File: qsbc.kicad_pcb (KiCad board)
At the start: 6 copper layers, 80 x 80 mm, 126 parts, among them J1 USB_C_Receptacle_USB2.0, J2 USB_C_Receptacle_USB2.0, J3 USB_C_Receptacle_USB2.0, J4 ARJM11D7-502-AB-EW2, J7 USB_C_Receptacle_USB2.0, J8 Bus_M.2_Socket_M, U1 MIMX8MM6DVTLZAA, U10 TUSB320LI, U11 CH343P, U12 TPD4EUSB30, U13 TPD4EUSB30, U14 TPD4EUSB30, U15 W25Q32JVZP, U16 BD71847MWV, U18 RTL8211F, U19 NX5P3363, U2 74LVC1G04, U21 INA231, U3 MT40A1G16KD-062E, U4 TPD4EUSB30, U5 NX5P3363, U6 TUSB320LI, U8 74LVC1G04, U9 TPD4EUSB30, Y1 Crystal

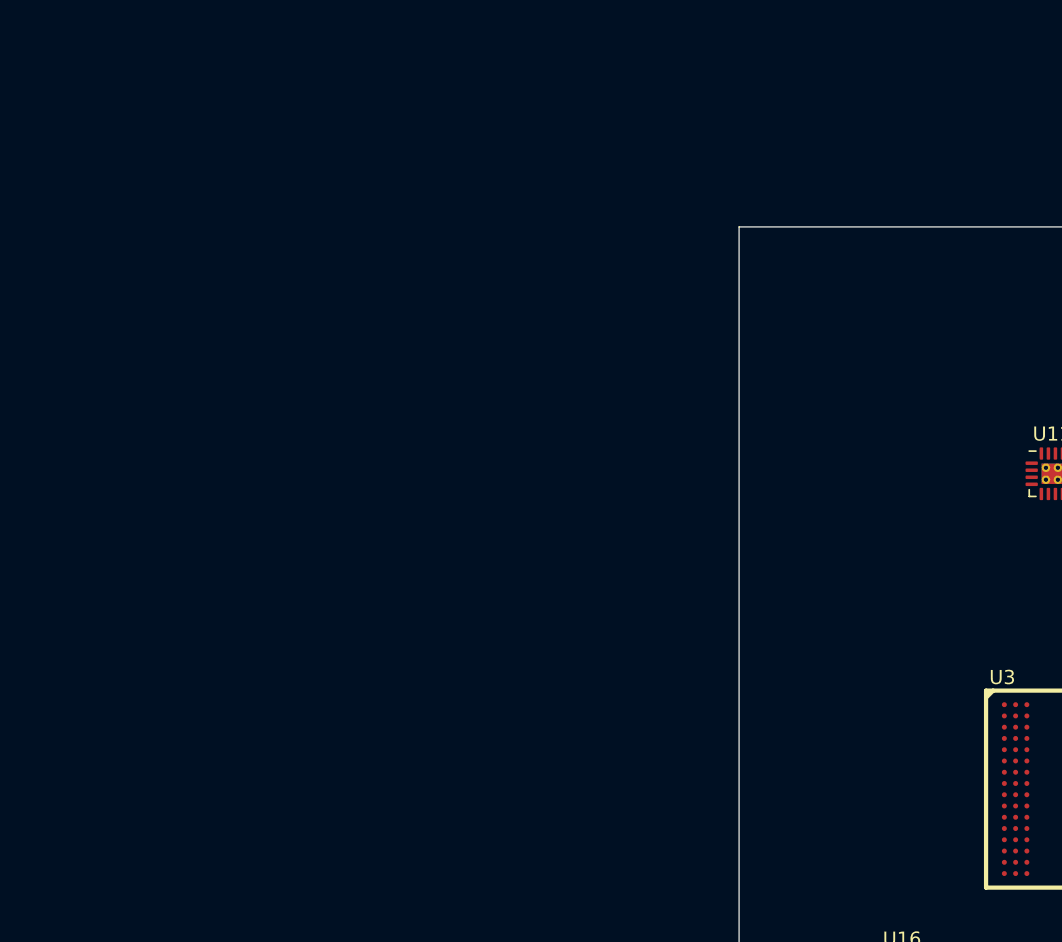
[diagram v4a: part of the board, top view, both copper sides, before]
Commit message: pcie done, misc fixes for usb, enet
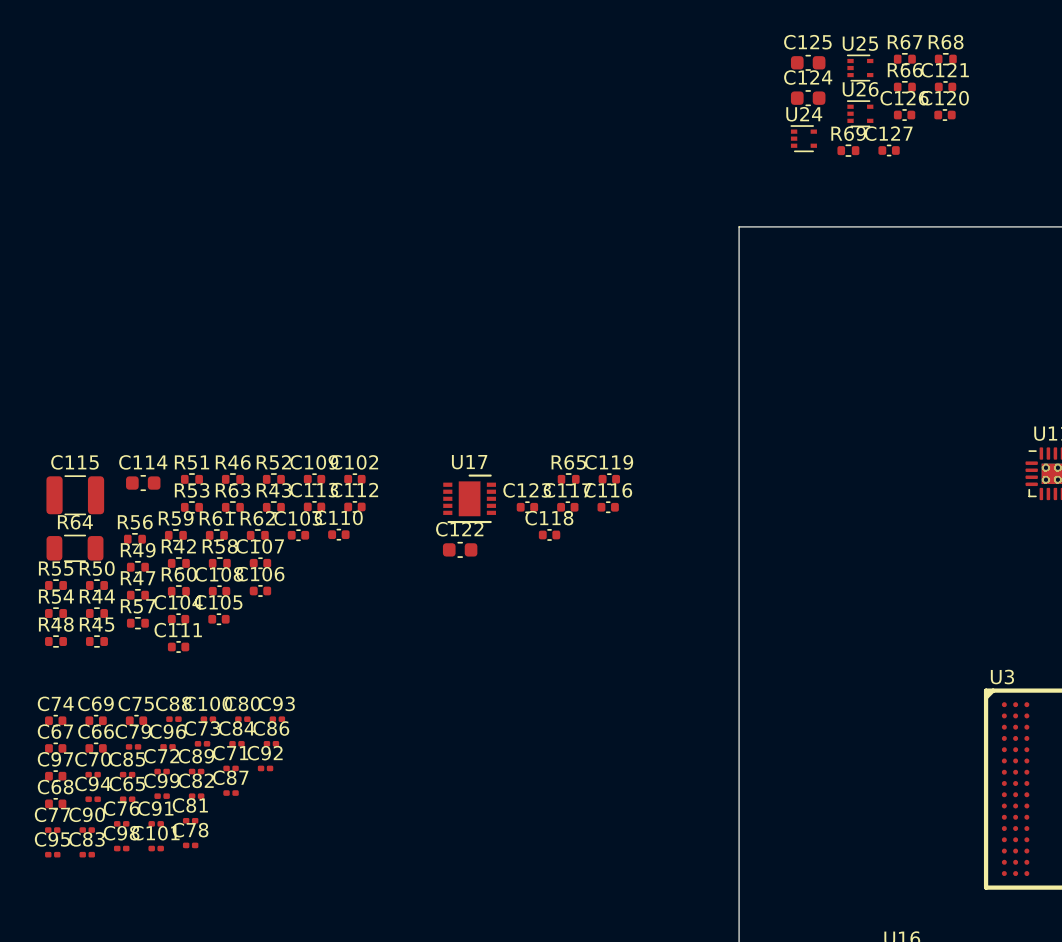
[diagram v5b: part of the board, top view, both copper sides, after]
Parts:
- added C100: 0.22uF, Capacitor_SMD:C_0201_0603Metric, F.Cu at (70.2, 93.9)
- added C101: 0.22uF, Capacitor_SMD:C_0201_0603Metric, F.Cu at (66.5, 103.1)
- added C102: 0.1uF, Capacitor_SMD:C_0402_1005Metric, F.Cu at (80.6, 76.9)
- added C103: 0.1uF, Capacitor_SMD:C_0402_1005Metric, F.Cu at (76.6, 80.8)
- added C104: 0.1uF, Capacitor_SMD:C_0402_1005Metric, F.Cu at (68.1, 86.8)
- added C105: 0.1uF, Capacitor_SMD:C_0402_1005Metric, F.Cu at (71.0, 86.8)
- added C106: 4.7uF, Capacitor_SMD:C_0402_1005Metric, F.Cu at (73.9, 84.8)
- added C107: 0.1uF, Capacitor_SMD:C_0402_1005Metric, F.Cu at (73.9, 82.8)
- added C108: 0.1uF, Capacitor_SMD:C_0402_1005Metric, F.Cu at (71.0, 84.8)
- added C109: 0.1uF, Capacitor_SMD:C_0402_1005Metric, F.Cu at (77.8, 76.9)
- added C110: C, Capacitor_SMD:C_0402_1005Metric, F.Cu at (79.5, 80.8)
- added C111: 0.1uF, Capacitor_SMD:C_0402_1005Metric, F.Cu at (68.1, 88.8)
- added C112: C, Capacitor_SMD:C_0402_1005Metric, F.Cu at (80.6, 78.8)
- added C113: 0.1uF, Capacitor_SMD:C_0402_1005Metric, F.Cu at (77.8, 78.8)
- added C114: 0.01uF, Capacitor_SMD:C_0603_1608Metric, F.Cu at (65.6, 77.1)
- added C115: 1000pF, Capacitor_SMD:C_1210_3225Metric, F.Cu at (60.8, 78.0)
- added C116: 4.7uF, Capacitor_SMD:C_0402_1005Metric, F.Cu at (98.6, 78.8)
- added C117: 0.1uF, Capacitor_SMD:C_0402_1005Metric, F.Cu at (95.8, 78.8)
- added C118: 20pF, Capacitor_SMD:C_0402_1005Metric, F.Cu at (94.5, 80.8)
- added C119: 20pF, Capacitor_SMD:C_0402_1005Metric, F.Cu at (98.7, 76.9)
- added C120: 0.22uF, Capacitor_SMD:C_0402_1005Metric, F.Cu at (122.6, 51.0)
- added C121: 0.22uF, Capacitor_SMD:C_0402_1005Metric, F.Cu at (122.6, 49.0)
- added C122: 10uF, Capacitor_SMD:C_0603_1608Metric, F.Cu at (88.1, 81.9)
- added C123: 0.1uF, Capacitor_SMD:C_0402_1005Metric, F.Cu at (92.9, 78.8)
- added C124: 10uF, Capacitor_SMD:C_0603_1608Metric, F.Cu at (112.8, 49.8)
- added C125: 10uF, Capacitor_SMD:C_0603_1608Metric, F.Cu at (112.8, 47.3)
- added C126: 0.1uF, Capacitor_SMD:C_0402_1005Metric, F.Cu at (119.7, 51.0)
- added C127: 0.1uF, Capacitor_SMD:C_0402_1005Metric, F.Cu at (118.6, 53.5)
- added C65: 1uF, Capacitor_SMD:C_0201_0603Metric, F.Cu at (64.5, 99.6)
- added C66: 10uF, Capacitor_SMD:C_0402_1005Metric, F.Cu at (62.2, 96.0)
- added C67: 10uF, Capacitor_SMD:C_0402_1005Metric, F.Cu at (59.4, 96.0)
- added C68: 10uF, Capacitor_SMD:C_0402_1005Metric, F.Cu at (59.4, 99.9)
- added C69: 10uF, Capacitor_SMD:C_0402_1005Metric, F.Cu at (62.2, 94.0)
- added C70: 1uF, Capacitor_SMD:C_0201_0603Metric, F.Cu at (62.0, 97.8)
- added C71: 0.22uF, Capacitor_SMD:C_0201_0603Metric, F.Cu at (71.8, 97.4)
- added C72: 1uF, Capacitor_SMD:C_0201_0603Metric, F.Cu at (66.9, 97.6)
- added C73: 1uF, Capacitor_SMD:C_0201_0603Metric, F.Cu at (69.8, 95.7)
- added C74: 10uF, Capacitor_SMD:C_0402_1005Metric, F.Cu at (59.4, 94.0)
- added C75: 10uF, Capacitor_SMD:C_0402_1005Metric, F.Cu at (65.1, 94.0)
- added C76: 1uF, Capacitor_SMD:C_0201_0603Metric, F.Cu at (64.1, 101.3)
- added C77: 1uF, Capacitor_SMD:C_0201_0603Metric, F.Cu at (59.2, 101.8)
- added C78: 1uF, Capacitor_SMD:C_0201_0603Metric, F.Cu at (69.0, 102.9)
- added C79: 1uF, Capacitor_SMD:C_0201_0603Metric, F.Cu at (64.9, 95.9)
- added C80: 0.22uF, Capacitor_SMD:C_0201_0603Metric, F.Cu at (72.7, 93.9)
- added C81: 1uF, Capacitor_SMD:C_0201_0603Metric, F.Cu at (69.0, 101.1)
- added C82: 1uF, Capacitor_SMD:C_0201_0603Metric, F.Cu at (69.4, 99.4)
- added C83: 1uF, Capacitor_SMD:C_0201_0603Metric, F.Cu at (61.6, 103.5)
- added C84: 1uF, Capacitor_SMD:C_0201_0603Metric, F.Cu at (72.3, 95.7)
- added C85: 1uF, Capacitor_SMD:C_0201_0603Metric, F.Cu at (64.5, 97.8)
- added C86: 1uF, Capacitor_SMD:C_0201_0603Metric, F.Cu at (74.7, 95.7)
- added C87: 1uF, Capacitor_SMD:C_0201_0603Metric, F.Cu at (71.8, 99.2)
- added C88: 1uF, Capacitor_SMD:C_0201_0603Metric, F.Cu at (67.8, 93.9)
- added C89: 1uF, Capacitor_SMD:C_0201_0603Metric, F.Cu at (69.4, 97.6)
- added C90: 1uF, Capacitor_SMD:C_0201_0603Metric, F.Cu at (61.6, 101.8)
- added C91: 1uF, Capacitor_SMD:C_0201_0603Metric, F.Cu at (66.5, 101.3)
- added C92: 1uF, Capacitor_SMD:C_0201_0603Metric, F.Cu at (74.3, 97.4)
- added C93: 1uF, Capacitor_SMD:C_0201_0603Metric, F.Cu at (75.1, 93.9)
- added C94: 1uF, Capacitor_SMD:C_0201_0603Metric, F.Cu at (62.0, 99.6)
- added C95: 1uF, Capacitor_SMD:C_0201_0603Metric, F.Cu at (59.2, 103.5)
- added C96: 1uF, Capacitor_SMD:C_0201_0603Metric, F.Cu at (67.4, 95.9)
- added C97: 10uF, Capacitor_SMD:C_0402_1005Metric, F.Cu at (59.4, 98.0)
- added C98: 0.22uF, Capacitor_SMD:C_0201_0603Metric, F.Cu at (64.1, 103.1)
- added C99: 0.22uF, Capacitor_SMD:C_0201_0603Metric, F.Cu at (66.9, 99.4)
- added R42: 4.7K, Resistor_SMD:R_0402_1005Metric, F.Cu at (68.1, 82.8)
- added R43: 4.7K, Resistor_SMD:R_0402_1005Metric, F.Cu at (74.9, 78.9)
- added R44: 4.7K, Resistor_SMD:R_0402_1005Metric, F.Cu at (62.3, 86.4)
- added R45: 4.7K, Resistor_SMD:R_0402_1005Metric, F.Cu at (62.3, 88.4)
- added R46: 4.7K, Resistor_SMD:R_0402_1005Metric, F.Cu at (72.0, 76.9)
- added R47: 4.7K, Resistor_SMD:R_0402_1005Metric, F.Cu at (65.2, 85.1)
- added R48: 4.7K, Resistor_SMD:R_0402_1005Metric, F.Cu at (59.4, 88.4)
- added R49: 4.7K, Resistor_SMD:R_0402_1005Metric, F.Cu at (65.2, 83.1)
- added R50: 4.7K, Resistor_SMD:R_0402_1005Metric, F.Cu at (62.3, 84.4)
- added R51: 1.5K, Resistor_SMD:R_0402_1005Metric, F.Cu at (69.1, 76.9)
- added R52: 0R, Resistor_SMD:R_0402_1005Metric, F.Cu at (74.9, 76.9)
- added R53: 0R, Resistor_SMD:R_0402_1005Metric, F.Cu at (69.1, 78.9)
- added R54: 0R, Resistor_SMD:R_0402_1005Metric, F.Cu at (59.4, 86.4)
- added R55: 0R, Resistor_SMD:R_0402_1005Metric, F.Cu at (59.4, 84.4)
- added R56: 0R, Resistor_SMD:R_0402_1005Metric, F.Cu at (65.0, 81.1)
- added R57: 2.49K, Resistor_SMD:R_0402_1005Metric, F.Cu at (65.2, 87.1)
- added R58: 4.7K, Resistor_SMD:R_0402_1005Metric, F.Cu at (71.0, 82.8)
- added R59: 4.7K, Resistor_SMD:R_0402_1005Metric, F.Cu at (67.9, 80.8)
- added R60: 4.7K, Resistor_SMD:R_0402_1005Metric, F.Cu at (68.1, 84.8)
- added R61: 4.7K, Resistor_SMD:R_0402_1005Metric, F.Cu at (70.8, 80.8)
- added R62: 470R, Resistor_SMD:R_0402_1005Metric, F.Cu at (73.7, 80.8)
- added R63: 470R, Resistor_SMD:R_0402_1005Metric, F.Cu at (72.0, 78.9)
- added R64: 1M, Resistor_SMD:R_1206_3216Metric, F.Cu at (60.8, 81.8)
- added R65: 8,2K, Resistor_SMD:R_0402_1005Metric, F.Cu at (95.8, 76.9)
- added R66: 10K, Resistor_SMD:R_0402_1005Metric, F.Cu at (119.7, 49.0)
- added R67: 10K, Resistor_SMD:R_0402_1005Metric, F.Cu at (119.7, 47.0)
- added R68: 10K, Resistor_SMD:R_0402_1005Metric, F.Cu at (122.6, 47.0)
- added R69: 10K, Resistor_SMD:R_0402_1005Metric, F.Cu at (115.7, 53.5)
- added U17: SI52112-B5-GM2, Package_DFN_QFN:DFN-10-1EP_3x3mm_P0.5mm_EP1.55x2.48mm, F.Cu at (88.8, 78.2)
- added U24: 74LVC1G07, Package_TO_SOT_SMD:SOT-553, F.Cu at (112.5, 52.7)
- added U25: 74LVC1G07, Package_TO_SOT_SMD:SOT-553, F.Cu at (116.6, 47.6)
- added U26: 74LVC1G07, Package_TO_SOT_SMD:SOT-553, F.Cu at (116.6, 50.9)
- U18: value RTL8211F -> RTL8211FD
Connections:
- net Net-(J8-Pad12) renamed VDD
- J4 pad 1: unconnected-(J4-Pad1) -> /Ethernet/TRD0_P
- J4 pad 10: unconnected-(J4-Pad10) -> /Ethernet/TRD3_N
- J4 pad 11: unconnected-(J4-Pad11) -> Net-(J4-Pad11)
- J4 pad 12: unconnected-(J4-Pad12) -> /Ethernet/ENET_LED2
- J4 pad 13: unconnected-(J4-Pad13) -> /Ethernet/ENET_LED1
- J4 pad 14: unconnected-(J4-Pad14) -> Net-(J4-Pad14)
- J4 pad 15: unconnected-(J4-Pad15) -> GNDPWR
- J4 pad 16: unconnected-(J4-Pad16) -> GNDPWR
- J4 pad 2: unconnected-(J4-Pad2) -> /Ethernet/TRD0_N
- J4 pad 3: unconnected-(J4-Pad3) -> /Ethernet/TRD1_P
- J4 pad 4: unconnected-(J4-Pad4) -> /Ethernet/TRD1_N
- J4 pad 5: unconnected-(J4-Pad5) -> Net-(J4-Pad5)
- J4 pad 6: unconnected-(J4-Pad6) -> Net-(J4-Pad5)
- J4 pad 7: unconnected-(J4-Pad7) -> /Ethernet/TRD2_P
- J4 pad 8: unconnected-(J4-Pad8) -> /Ethernet/TRD2_N
- J4 pad 9: unconnected-(J4-Pad9) -> /Ethernet/TRD3_P
- J8 pad 41: unconnected-(J8-Pad41) -> /PCIe/PCIE_RX_N
- J8 pad 43: unconnected-(J8-Pad43) -> /PCIe/PCIE_RX_P
- J8 pad 47: unconnected-(J8-Pad47) -> /PCIe/PCIE_TX_R_P
- J8 pad 49: unconnected-(J8-Pad49) -> /PCIe/PCIE_TX_R_N
- J8 pad 50: unconnected-(J8-Pad50) -> /PCIe/~{PCIE_RESET_3.3V}
- J8 pad 52: unconnected-(J8-Pad52) -> Net-(J8-Pad52)
- J8 pad 53: unconnected-(J8-Pad53) -> /PCIe/M2_REFCLK_N
- J8 pad 54: unconnected-(J8-Pad54) -> Net-(J8-Pad54)
- J8 pad 55: unconnected-(J8-Pad55) -> /PCIe/M2_REFCLK_P
- J8 pad 69: unconnected-(J8-Pad69) -> Net-(J8-Pad69)
- U1 pad A19: unconnected-(U1-PadA19) -> /PCIe/PCIE_RX_N
- U1 pad A20: unconnected-(U1-PadA20) -> /PCIe/PCIE_TX_N
- U1 pad A21: unconnected-(U1-PadA21) -> /PCIe/PCIE_REFCLK_P
- U1 pad AB27: unconnected-(U1-PadAB27) -> /Ethernet/ENET_MDIO
- U1 pad AC26: unconnected-(U1-PadAC26) -> /Ethernet/ENET_RD3
- U1 pad AC27: unconnected-(U1-PadAC27) -> /Ethernet/ENET_MDC
- U1 pad AD26: unconnected-(U1-PadAD26) -> /Ethernet/ENET_RD2
- U1 pad AD27: unconnected-(U1-PadAD27) -> /Ethernet/ENET_RD1
- U1 pad AE26: unconnected-(U1-PadAE26) -> /Ethernet/ENET_RXC
- U1 pad AE27: unconnected-(U1-PadAE27) -> /Ethernet/ENET_RD0
- U1 pad AF24: unconnected-(U1-PadAF24) -> /Ethernet/ENET_TX_CTL
- U1 pad AF25: unconnected-(U1-PadAF25) -> /Ethernet/ENET_TD3
- U1 pad AF26: unconnected-(U1-PadAF26) -> /Ethernet/ENET_TD1
- U1 pad AF27: unconnected-(U1-PadAF27) -> /Ethernet/ENET_RX_CTL
- U1 pad AG24: unconnected-(U1-PadAG24) -> /Ethernet/ENET_TXC
- U1 pad AG25: unconnected-(U1-PadAG25) -> /Ethernet/ENET_TD2
- U1 pad AG26: unconnected-(U1-PadAG26) -> /Ethernet/ENET_TD0
- U1 pad B19: unconnected-(U1-PadB19) -> /PCIe/PCIE_RX_P
- U1 pad B20: unconnected-(U1-PadB20) -> /PCIe/PCIE_TX_P
- U1 pad B21: unconnected-(U1-PadB21) -> /PCIe/PCIE_REFCLK_N
- U1 pad D19: unconnected-(U1-PadD19) -> /PCIe/PCIE_RESREF
- U1 pad J10: unconnected-(U1-PadJ10) -> /i.MX8MM Power/VDD_DRAM_xPU_0.9V
- U1 pad J11: unconnected-(U1-PadJ11) -> /i.MX8MM Power/NVCC_1.8V
- U1 pad J12: unconnected-(U1-PadJ12) -> /i.MX8MM Power/NVCC_1.8V
- U1 pad J22: unconnected-(U1-PadJ22) -> /i.MX8MM Power/NVCC_SNVS_1.8V
- U1 pad K12: unconnected-(U1-PadK12) -> /i.MX8MM Power/VDD_DRAM_xPU_0.9V
- U1 pad K13: unconnected-(U1-PadK13) -> /i.MX8MM Power/VDD_DRAM_xPU_0.9V
- U1 pad K15: /i.MX8MM Power/NVCC_DRAM -> /i.MX8MM Power/VDD_SOC_0.8V
- U1 pad K16: /i.MX8MM Power/NVCC_DRAM -> /i.MX8MM Power/VDD_SOC_0.8V
- U1 pad K22: unconnected-(U1-PadK22) -> /i.MX8MM Power/VDD_SNVS_0.8V
- U1 pad K8: unconnected-(U1-PadK8) -> /i.MX8MM Power/NVCC_DRAM_1.2V
- U1 pad K9: unconnected-(U1-PadK9) -> /i.MX8MM Power/NVCC_DRAM_1.2V
- U1 pad L10: unconnected-(U1-PadL10) -> /i.MX8MM Power/VDD_DRAM_xPU_0.9V
- U1 pad L11: unconnected-(U1-PadL11) -> /i.MX8MM Power/VDD_DRAM_xPU_0.9V
- U1 pad L13: unconnected-(U1-PadL13) -> /i.MX8MM Power/VDD_DRAM_xPU_0.9V
- U1 pad L15: /i.MX8MM Power/NVCC_DRAM -> /i.MX8MM Power/VDD_SOC_0.8V
- U1 pad L18: unconnected-(U1-PadL18) -> /i.MX8MM Power/VDD_SOC_0.8V
- U1 pad L19: unconnected-(U1-PadL19) -> /i.MX8MM Power/NVCC_1.8V
- U1 pad L9: unconnected-(U1-PadL9) -> /i.MX8MM Power/NVCC_DRAM_1.2V
- U1 pad M13: unconnected-(U1-PadM13) -> /i.MX8MM Power/VDD_DRAM_xPU_0.9V
- U1 pad M14: unconnected-(U1-PadM14) -> /i.MX8MM Power/VDD_DRAM_xPU_0.9V
- U1 pad M15: /i.MX8MM Power/NVCC_DRAM -> /i.MX8MM Power/VDD_SOC_0.8V
- U1 pad M19: unconnected-(U1-PadM19) -> /i.MX8MM Power/NVCC_1.8V
- U1 pad M9: unconnected-(U1-PadM9) -> /i.MX8MM Power/NVCC_DRAM_1.2V
- U1 pad N10: unconnected-(U1-PadN10) -> /i.MX8MM Power/VDD_DRAM_xPU_0.9V
- U1 pad N11: unconnected-(U1-PadN11) -> /i.MX8MM Power/VDD_DRAM_xPU_0.9V
- U1 pad N13: unconnected-(U1-PadN13) -> /i.MX8MM Power/VDD_SOC_0.8V
- U1 pad N15: /i.MX8MM Power/NVCC_DRAM -> /i.MX8MM Power/VDD_SOC_0.8V
- U1 pad N18: /i.MX8MM Power/VDD_SOC -> /i.MX8MM Power/VDD_SOC_0.8V
- U1 pad N19: unconnected-(U1-PadN19) -> /i.MX8MM Power/VDDA_1.8V
- U1 pad N8: unconnected-(U1-PadN8) -> /i.MX8MM Power/NVCC_DRAM_1.2V
- U1 pad N9: unconnected-(U1-PadN9) -> /i.MX8MM Power/NVCC_DRAM_1.2V
- U1 pad P12: unconnected-(U1-PadP12) -> /i.MX8MM Power/VDD_DRAM_xPU_0.9V
- U1 pad P5: unconnected-(U1-PadP5) -> /i.MX8MM Power/VDDA_1.8V
- U1 pad P7: unconnected-(U1-PadP7) -> /i.MX8MM Power/NVCC_DRAM_1.2V
- U1 pad P9: unconnected-(U1-PadP9) -> /i.MX8MM Power/VDD_DRAM_xPU_0.9V
- U1 pad R10: unconnected-(U1-PadR10) -> /i.MX8MM Power/VDD_DRAM_xPU_0.9V
- U1 pad R11: unconnected-(U1-PadR11) -> /i.MX8MM Power/VDD_DRAM_xPU_0.9V
- U1 pad R13: /i.MX8MM Power/VDD_SOC -> /i.MX8MM Power/VDD_ARM_0.9V
- U1 pad R15: /i.MX8MM Power/VDD_SOC -> /i.MX8MM Power/VDD_ARM_0.9V
- U1 pad R17: /i.MX8MM Power/NVCC_DRAM -> /i.MX8MM Power/VDD_SOC_0.8V
- U1 pad R18: /i.MX8MM Power/VDD_SOC -> /i.MX8MM Power/VDD_SOC_0.8V
- U1 pad R8: unconnected-(U1-PadR8) -> /i.MX8MM Power/NVCC_DRAM_1.2V
- U1 pad R9: unconnected-(U1-PadR9) -> /i.MX8MM Power/NVCC_DRAM_1.2V
- U1 pad T13: /i.MX8MM Power/VDD_SOC -> /i.MX8MM Power/VDD_ARM_0.9V
- U1 pad T14: /i.MX8MM Power/VDD_SOC -> /i.MX8MM Power/VDD_ARM_0.9V
- U1 pad T15: /i.MX8MM Power/VDD_SOC -> /i.MX8MM Power/VDD_ARM_0.9V
- U1 pad T9: unconnected-(U1-PadT9) -> /i.MX8MM Power/NVCC_DRAM_1.2V
- U1 pad U10: unconnected-(U1-PadU10) -> /i.MX8MM Power/VDD_DRAM_xPU_0.9V
- U1 pad U11: unconnected-(U1-PadU11) -> /i.MX8MM Power/VDD_DRAM_xPU_0.9V
- U1 pad U13: /i.MX8MM Power/VDD_SOC -> /i.MX8MM Power/VDD_ARM_0.9V
- U1 pad U15: /i.MX8MM Power/VDD_SOC -> /i.MX8MM Power/VDD_ARM_0.9V
- U1 pad U17: /i.MX8MM Power/NVCC_DRAM -> /i.MX8MM Power/VDD_SOC_0.8V
- U1 pad U18: /i.MX8MM Power/VDD_SOC -> /i.MX8MM Power/VDD_SOC_0.8V
- U1 pad U9: unconnected-(U1-PadU9) -> /i.MX8MM Power/NVCC_DRAM_1.2V
- U1 pad V12: unconnected-(U1-PadV12) -> /i.MX8MM Power/VDD_DRAM_xPU_0.9V
- U1 pad V13: /i.MX8MM Power/VDD_SOC -> /i.MX8MM Power/VDD_ARM_0.9V
- U1 pad V15: /i.MX8MM Power/VDD_SOC -> /i.MX8MM Power/VDD_ARM_0.9V
- U1 pad V16: /i.MX8MM Power/VDD_SOC -> /i.MX8MM Power/VDD_ARM_0.9V
- U1 pad V19: unconnected-(U1-PadV19) -> /i.MX8MM Power/NVCC_1.8V
- U1 pad V20: unconnected-(U1-PadV20) -> /i.MX8MM Power/NVCC_1.8V
- U1 pad V8: unconnected-(U1-PadV8) -> /i.MX8MM Power/NVCC_DRAM_1.2V
- U1 pad V9: unconnected-(U1-PadV9) -> /i.MX8MM Power/NVCC_DRAM_1.2V
- U1 pad W10: unconnected-(U1-PadW10) -> /i.MX8MM Power/VDD_DRAM_xPU_0.9V
- U1 pad W11: unconnected-(U1-PadW11) -> /i.MX8MM Power/VDD_DRAM_xPU_0.9V
- U1 pad W12: unconnected-(U1-PadW12) -> /i.MX8MM Power/NVCC_1.8V
- U1 pad W13: /i.MX8MM Power/VDD_SOC -> /i.MX8MM Power/VDD_ARM_0.9V
- U1 pad W14: /i.MX8MM Power/VDD_SOC -> /i.MX8MM Power/VDD_ARM_0.9V
- U1 pad W15: /i.MX8MM Power/VDD_SOC -> /i.MX8MM Power/VDD_ARM_0.9V
- U1 pad W16: /i.MX8MM Power/VDD_SOC -> /i.MX8MM Power/VDD_ARM_0.9V
- U13 pad 1: Net-(U13-Pad1) -> /Ethernet/TRD2_P
- U13 pad 10: Net-(U13-Pad1) -> /Ethernet/TRD2_P
- U13 pad 2: Net-(U13-Pad2) -> /Ethernet/TRD2_N
- U13 pad 3: Net-(U13-Pad3) -> GND
- U13 pad 4: Net-(U13-Pad4) -> /Ethernet/TRD3_P
- U13 pad 5: Net-(U13-Pad5) -> /Ethernet/TRD3_N
- U13 pad 6: Net-(U13-Pad5) -> /Ethernet/TRD3_N
- U13 pad 7: Net-(U13-Pad4) -> /Ethernet/TRD3_P
- U13 pad 8: Net-(U13-Pad3) -> GND
- U13 pad 9: Net-(U13-Pad2) -> /Ethernet/TRD2_N
- U14 pad 1: Net-(U14-Pad1) -> /Ethernet/TRD0_P
- U14 pad 10: Net-(U14-Pad1) -> /Ethernet/TRD0_P
- U14 pad 2: Net-(U14-Pad2) -> /Ethernet/TRD0_N
- U14 pad 3: Net-(U14-Pad3) -> GND
- U14 pad 4: Net-(U14-Pad4) -> /Ethernet/TRD1_P
- U14 pad 5: Net-(U14-Pad5) -> /Ethernet/TRD1_N
- U14 pad 6: Net-(U14-Pad5) -> /Ethernet/TRD1_N
- U14 pad 7: Net-(U14-Pad4) -> /Ethernet/TRD1_P
- U14 pad 8: Net-(U14-Pad3) -> GND
- U14 pad 9: Net-(U14-Pad2) -> /Ethernet/TRD0_N
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
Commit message: ddr: add dual die support, misc work
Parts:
- added C128: 0.1uF, Capacitor_SMD:C_0402_1005Metric, F.Cu at (314.2, 207.7)
- added C129: 0.1uF, Capacitor_SMD:C_0402_1005Metric, F.Cu at (320.1, 203.8)
- added C130: 0.1uF, Capacitor_SMD:C_0402_1005Metric, F.Cu at (318.4, 205.8)
- added C131: 18pF, Capacitor_SMD:C_0402_1005Metric, F.Cu at (320.2, 216.1)
- added C132: 10uF, Capacitor_SMD:C_0402_1005Metric, F.Cu at (315.0, 214.4)
- added C133: 0.1uF, Capacitor_SMD:C_0402_1005Metric, F.Cu at (313.1, 220.6)
- added C134: 0.1uF, Capacitor_SMD:C_0402_1005Metric, F.Cu at (316.0, 218.7)
- added C135: 1uF, Capacitor_SMD:C_0402_1005Metric, F.Cu at (317.3, 216.7)
- added C136: 0.1uF, Capacitor_SMD:C_0402_1005Metric, F.Cu at (316.0, 220.6)
- added C137: 0.1uF, Capacitor_SMD:C_0402_1005Metric, F.Cu at (329.8, 216.7)
- added C138: 0.1uF, Capacitor_SMD:C_0402_1005Metric, F.Cu at (329.8, 218.7)
- added C139: 0.22uF, Capacitor_SMD:C_0201_0603Metric, F.Cu at (317.1, 254.5)
- added C140: 10uF, Capacitor_SMD:C_0402_1005Metric, F.Cu at (314.4, 254.6)
- added C141: 0.22uF, Capacitor_SMD:C_0201_0603Metric, F.Cu at (319.1, 256.3)
- added C142: 0.22uF, Capacitor_SMD:C_0201_0603Metric, F.Cu at (319.5, 254.5)
- added C143: 0.22uF, Capacitor_SMD:C_0201_0603Metric, F.Cu at (316.7, 256.5)
- added C144: 0.22uF, Capacitor_SMD:C_0201_0603Metric, F.Cu at (314.2, 256.5)
- added C145: 2200pF, Capacitor_SMD:C_0402_1005Metric, F.Cu at (361.6, 181.5)
- added C146: 0.22uF, Capacitor_SMD:C_0201_0603Metric, F.Cu at (369.1, 181.2)
- added C147: 10uF, Capacitor_SMD:C_0402_1005Metric, F.Cu at (361.6, 179.5)
- added C148: 4.7uF, Capacitor_SMD:C_0402_1005Metric, F.Cu at (364.4, 179.5)
- added C149: 0.22uF, Capacitor_SMD:C_0201_0603Metric, F.Cu at (363.8, 185.1)
- added C150: 0.22uF, Capacitor_SMD:C_0201_0603Metric, F.Cu at (363.8, 183.3)
- added C151: 0.22uF, Capacitor_SMD:C_0201_0603Metric, F.Cu at (367.1, 179.4)
- added C152: 0.22uF, Capacitor_SMD:C_0201_0603Metric, F.Cu at (361.4, 185.1)
- added C153: 0.22uF, Capacitor_SMD:C_0201_0603Metric, F.Cu at (361.4, 183.3)
- added C154: 0.22uF, Capacitor_SMD:C_0201_0603Metric, F.Cu at (364.2, 181.4)
- added C155: 0.22uF, Capacitor_SMD:C_0201_0603Metric, F.Cu at (366.7, 181.4)
- added C156: 0.22uF, Capacitor_SMD:C_0201_0603Metric, F.Cu at (366.3, 183.1)
- added C157: 0.22uF, Capacitor_SMD:C_0201_0603Metric, F.Cu at (369.6, 179.4)
- added C158: 0.22uF, Capacitor_SMD:C_0201_0603Metric, F.Cu at (366.3, 184.9)
- added C159: 12pF, Capacitor_SMD:C_0402_1005Metric, F.Cu at (333.3, 272.9)
- added C160: 12pF, Capacitor_SMD:C_0402_1005Metric, F.Cu at (330.2, 276.9)
- added C19: 10uF, Capacitor_SMD:C_0603_1608Metric, F.Cu at (290.1, 234.1)
- added C20: 10uF, Capacitor_SMD:C_0603_1608Metric, F.Cu at (278.0, 231.6)
- added C21: 10uF, Capacitor_SMD:C_0603_1608Metric, F.Cu at (282.0, 239.1)
- added C22: 10uF, Capacitor_SMD:C_0603_1608Metric, F.Cu at (278.0, 234.1)
- added C23: 10uF, Capacitor_SMD:C_0603_1608Metric, F.Cu at (278.0, 236.6)
- added C24: 10uF, Capacitor_SMD:C_0603_1608Metric, F.Cu at (294.1, 231.6)
- added C25: 10uF, Capacitor_SMD:C_0603_1608Metric, F.Cu at (286.0, 241.6)
- added C26: 10uF, Capacitor_SMD:C_0603_1608Metric, F.Cu at (286.0, 239.1)
- added C33: 10uF, Capacitor_SMD:C_0603_1608Metric, F.Cu at (282.0, 231.6)
- added C34: 22uF, Capacitor_SMD:C_0603_1608Metric, F.Cu at (278.0, 239.1)
- added C35: 22uF, Capacitor_SMD:C_0603_1608Metric, F.Cu at (282.0, 236.6)
- added C36: 22uF, Capacitor_SMD:C_0603_1608Metric, F.Cu at (290.1, 231.6)
- added C37: 22uF, Capacitor_SMD:C_0603_1608Metric, F.Cu at (286.0, 231.6)
- added C38: 22uF, Capacitor_SMD:C_0603_1608Metric, F.Cu at (294.1, 234.1)
- added C39: 22uF, Capacitor_SMD:C_0603_1608Metric, F.Cu at (286.0, 236.6)
- added C40: 22uF, Capacitor_SMD:C_0603_1608Metric, F.Cu at (278.0, 241.6)
- added C41: 22uF, Capacitor_SMD:C_0603_1608Metric, F.Cu at (298.1, 231.6)
- added C42: 22uF, Capacitor_SMD:C_0603_1608Metric, F.Cu at (286.0, 234.1)
- added C43: 22uF, Capacitor_SMD:C_0603_1608Metric, F.Cu at (290.1, 236.6)
- added C44: 22uF, Capacitor_SMD:C_0603_1608Metric, F.Cu at (282.0, 234.1)
- added C46: 22uF, Capacitor_SMD:C_0603_1608Metric, F.Cu at (282.0, 241.6)
- added D2: LED_Orange, LED_SMD:LED_0603_1608Metric, F.Cu at (307.9, 207.4)
- added D3: LED_Yellow, LED_SMD:LED_0603_1608Metric, F.Cu at (327.4, 214.5)
- added H1: MountingHole_Pad, MountingHole:MountingHole_3.2mm_M3_Pad_Via, F.Cu at (111.9, 134.9)
- added H2: MountingHole_Pad, MountingHole:MountingHole_3.2mm_M3_Pad_Via, F.Cu at (183.9, 134.9)
- added H3: MountingHole_Pad, MountingHole:MountingHole_3.2mm_M3_Pad_Via, F.Cu at (111.9, 62.9)
- added H4: MountingHole_Pad, MountingHole:MountingHole_3.2mm_M3_Pad_Via, F.Cu at (183.9, 62.9)
- added H5: MountingHole_Pad, Mounting_Wuerth:Mounting_Wuerth_WA-SMSI-M3_H2.5mm_9774025360, F.Cu at (168.1, 101.3)
- added J5: Micro_SD_Card_Det1, qsbc:GCT_MEM2051-00-195-00-A_REVC, F.Cu at (139.4, 68.0)
- added J6: Conn_ARM_JTAG_SWD_10, Connector_PinHeader_1.27mm:PinHeader_2x05_P1.27mm_Vertical, F.Cu at (327.6, 202.5)
- added R1: 240R, Resistor_SMD:R_0201_0603Metric, F.Cu at (317.0, 232.9)
- added R10: 100K, Resistor_SMD:R_0402_1005Metric, F.Cu at (293.5, 236.3)
- added R100: 10K, Resistor_SMD:R_0402_1005Metric, F.Cu at (264.2, 156.4)
- added R101: 100K, Resistor_SMD:R_0402_1005Metric, F.Cu at (292.4, 238.8)
- added R102: 0R, Resistor_SMD:R_0402_1005Metric, F.Cu at (312.4, 270.9)
- added R103: 0R, Resistor_SMD:R_0402_1005Metric, F.Cu at (309.3, 277.0)
- added R104: 100K, Resistor_SMD:R_0402_1005Metric, F.Cu at (330.4, 270.9)
- added R105: 100K, Resistor_SMD:R_0402_1005Metric, F.Cu at (327.3, 277.0)
- added R106: 0R, Resistor_SMD:R_0402_1005Metric, F.Cu at (330.4, 274.9)
- added R107: 510K, Resistor_SMD:R_0402_1005Metric, F.Cu at (327.5, 272.9)
- added R108: 100K, Resistor_SMD:R_0402_1005Metric, F.Cu at (330.4, 272.9)
- added R109: 100K, Resistor_SMD:R_0402_1005Metric, F.Cu at (327.5, 274.9)
- added R11: 100K, Resistor_SMD:R_0402_1005Metric, F.Cu at (297.5, 233.8)
- added R110: 10K, Resistor_SMD:R_0402_1005Metric, F.Cu at (327.5, 270.9)
- added R111: 100K, Resistor_SMD:R_0402_1005Metric, F.Cu at (324.4, 277.0)
- added R112: 10K, Resistor_SMD:R_0402_1005Metric, F.Cu at (333.3, 270.9)
- added R113: 4.7K, Resistor_SMD:R_0402_1005Metric, F.Cu at (301.6, 286.4)
- added R114: 4.7K, Resistor_SMD:R_0402_1005Metric, F.Cu at (298.7, 286.4)
- added R15: 0R, Resistor_SMD:R_0402_1005Metric, F.Cu at (280.4, 252.5)
- added R16: 0R, Resistor_SMD:R_0402_1005Metric, F.Cu at (287.8, 248.1)
- added R2: 240R, Resistor_SMD:R_0201_0603Metric, F.Cu at (317.0, 231.2)
- added R22: 0R, Resistor_SMD:R_0402_1005Metric, F.Cu at (277.5, 254.5)
- added R23: 0R, Resistor_SMD:R_0402_1005Metric, F.Cu at (277.5, 252.5)
- added R70: 2.2K, Resistor_SMD:R_0402_1005Metric, F.Cu at (320.1, 201.8)
- added R71: 10K, Resistor_SMD:R_0402_1005Metric, F.Cu at (315.5, 205.7)
- added R72: 10K, Resistor_SMD:R_0402_1005Metric, F.Cu at (318.5, 214.2)
- added R73: 10K, Resistor_SMD:R_0402_1005Metric, F.Cu at (314.4, 216.7)
- added R74: 0R, Resistor_SMD:R_0402_1005Metric, F.Cu at (310.2, 218.2)
- added R75: 10K, Resistor_SMD:R_0402_1005Metric, F.Cu at (313.1, 218.7)
- added R76: 10K, Resistor_SMD:R_0402_1005Metric, F.Cu at (310.2, 220.2)
- added R77: 10K, Resistor_SMD:R_0402_1005Metric, F.Cu at (332.5, 201.8)
- added R78: 4.7K, Resistor_SMD:R_0402_1005Metric, F.Cu at (344.4, 201.8)
- added R79: 4.7K, Resistor_SMD:R_0402_1005Metric, F.Cu at (341.5, 201.8)
- added R80: 2.2K, Resistor_SMD:R_0402_1005Metric, F.Cu at (326.9, 216.8)
- added R81: 10K, Resistor_SMD:R_0402_1005Metric, F.Cu at (330.9, 214.2)
- added R82: 10K, Resistor_SMD:R_0402_1005Metric, F.Cu at (326.9, 218.7)
- added R83: 10K, Resistor_SMD:R_0402_1005Metric, F.Cu at (351.7, 191.2)
- added R84: 10K, Resistor_SMD:R_0402_1005Metric, F.Cu at (348.8, 191.2)
- added R85: 10K, Resistor_SMD:R_0402_1005Metric, F.Cu at (264.2, 154.4)
- added R86: 10K, Resistor_SMD:R_0402_1005Metric, F.Cu at (267.1, 152.4)
- added R87: 10K, Resistor_SMD:R_0402_1005Metric, F.Cu at (261.2, 152.4)
- added R88: 10K, Resistor_SMD:R_0402_1005Metric, F.Cu at (255.4, 154.4)
- added R89: 10K, Resistor_SMD:R_0402_1005Metric, F.Cu at (261.2, 154.4)
- added R9: 1M, Resistor_SMD:R_0402_1005Metric, F.Cu at (289.5, 238.8)
- added R90: 10K, Resistor_SMD:R_0402_1005Metric, F.Cu at (261.2, 158.4)
- added R91: 10K, Resistor_SMD:R_0402_1005Metric, F.Cu at (258.3, 154.4)
- added R92: 10K, Resistor_SMD:R_0402_1005Metric, F.Cu at (255.4, 156.4)
- added R93: 10K, Resistor_SMD:R_0402_1005Metric, F.Cu at (258.3, 152.4)
- added R94: 10K, Resistor_SMD:R_0402_1005Metric, F.Cu at (255.4, 152.4)
- added R95: 10K, Resistor_SMD:R_0402_1005Metric, F.Cu at (261.2, 156.4)
- added R96: 10K, Resistor_SMD:R_0402_1005Metric, F.Cu at (258.3, 158.4)
- added R97: 10K, Resistor_SMD:R_0402_1005Metric, F.Cu at (258.3, 156.4)
- added R98: 10K, Resistor_SMD:R_0402_1005Metric, F.Cu at (264.2, 152.4)
- added R99: 10K, Resistor_SMD:R_0402_1005Metric, F.Cu at (255.4, 158.4)
- added SW1: SW_DIP_x02, qsbc:DHN-02, F.Cu at (183.5, 92.2)
- added SW2: SW_Push, Button_Switch_THT:SW_Tactile_SPST_Angled_PTS645Vx58-2LFS, F.Cu at (300.3, 276.3)
- added TP22: TestPoint, TestPoint:TestPoint_Pad_D1.0mm, F.Cu at (309.4, 271.4)
- added TP23: TestPoint, TestPoint:TestPoint_Pad_D1.0mm, F.Cu at (309.4, 274.5)
- added TP24: TestPoint, TestPoint:TestPoint_Pad_D1.0mm, F.Cu at (321.4, 277.5)
- added TP25: TestPoint, TestPoint:TestPoint_Pad_D1.0mm, F.Cu at (324.5, 274.5)
- added TP26: TestPoint, TestPoint:TestPoint_Pad_D1.0mm, F.Cu at (324.5, 271.4)
- added TP27: TestPoint, TestPoint:TestPoint_Pad_D1.0mm, F.Cu at (321.4, 274.5)
- added TP28: TestPoint, TestPoint:TestPoint_Pad_D1.0mm, F.Cu at (321.4, 271.4)
- added U20: D5V0H1B2LP, qsbc:DFN100X60X45-2N, F.Cu at (280.4, 254.7)
- added U22: D5V0H1B2LP, qsbc:DFN100X60X45-2N, F.Cu at (283.3, 252.7)
- added U23: D5V0H1B2LP, qsbc:DFN100X60X45-2N, F.Cu at (287.8, 250.2)
- added U27: 74LVC1G07, Package_TO_SOT_SMD:SOT-23-5, F.Cu at (278.6, 249.3)
- added U28: TS3USB221E, Package_DFN_QFN:Texas_R-PUQFN-N10, F.Cu at (316.9, 202.8)
- added U29: TPD4EUSB30, Package_SON:USON-10_2.5x1.0mm_P0.5mm, F.Cu at (311.4, 208.1)
- added U30: TPD4EUSB30, Package_SON:USON-10_2.5x1.0mm_P0.5mm, F.Cu at (311.6, 215.2)
- added U31: D5V0H1B2LP, qsbc:DFN100X60X45-2N, F.Cu at (308.4, 247.5)
- added U32: SiP32431DR3, Package_TO_SOT_SMD:SOT-363_SC-70-6, F.Cu at (308.0, 215.1)
- added U33: TPD4EUSB30, Package_SON:USON-10_2.5x1.0mm_P0.5mm, F.Cu at (307.3, 219.0)
- added U7: D5V0H1B2LP, qsbc:DFN100X60X45-2N, F.Cu at (286.2, 252.7)
- added Y2: 25MHz, Crystal:Crystal_SMD_3225-4Pin_3.2x2.5mm, F.Cu at (306.1, 240.7)
- added Y3: 25MHz, Crystal:Crystal_SMD_3225-4Pin_3.2x2.5mm, F.Cu at (297.3, 249.3)
- added Y4: 24Mhz, Crystal:Crystal_SMD_3225-4Pin_3.2x2.5mm, F.Cu at (306.1, 232.5)
- C110, C112: value C -> 27pF
- C122, C124, C125: footprint Capacitor_SMD:C_0603_1608Metric -> Capacitor_SMD:C_0402_1005Metric
- C60, C61: footprint Capacitor_SMD:C_0402_1005Metric -> Capacitor_SMD:C_0201_0603Metric
- D1: value LED YELLOW -> LED_Yellow; footprint LED_SMD:LED_0402_1005Metric -> LED_SMD:LED_0603_1608Metric
- R17, R24: footprint Resistor_SMD:R_0402_1005Metric -> Resistor_SMD:R_0201_0603Metric
- R65: value 8,2K -> 8.2K
- U10, U6: value TUSB320LI -> TUSB320LAI
- U15: value W25Q32JVZP -> W25Q32JWZP
- U24, U25, U26: footprint Package_TO_SOT_SMD:SOT-553 -> Package_TO_SOT_SMD:SOT-23-5
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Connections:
- net Net-(J8-Pad52) renamed /PCIe/~{M2_CLKREQ_3.3V}
- C10 pad 1: /DDR/VCC_DRAM_1.2V -> /DDR/NVCC_DRAM_1.2V
- C100 pad 1: /i.MX8MM Power/NVCC_1.8V -> VCC
- C101 pad 1: /i.MX8MM Power/NVCC_1.8V -> VCC
- C11 pad 1: /DDR/VPP_2.5V -> /DDR/NVCC_DRAM_1.2V
- C16 pad 1: /Power/VDD_1.8V -> VCC
- C17 pad 1: /Power/VDD_3.3V -> VDD
- C18 pad 1: /Power/VDD_1.8V -> VCC
- C2 pad 1: /DDR/VCC_DRAM_1.2V -> /DDR/NVCC_DRAM_1.2V
- C27 pad 1: /Power/NVCC_SNVS_1P8 -> /Misc/NVCC_SNVS_1.8V
- C28 pad 1: /Power/VDD_SNVS_0.8V -> /Misc/VDD_SNVS_0.8V
- C3 pad 1: /DDR/VCC_DRAM_1.2V -> /DDR/NVCC_DRAM_1.2V
- C4 pad 1: /DDR/VCC_DRAM_1.2V -> /DDR/NVCC_DRAM_1.2V
- C48 pad 1: /Power/NVCC_SNVS_1P8 -> /Misc/NVCC_SNVS_1.8V
- C5 pad 1: /DDR/VCC_DRAM_1.2V -> /DDR/NVCC_DRAM_1.2V
- C50 pad 1: /USB/VSYS_5V -> /Power/VSYS_5V
- C53 pad 1: /USB/VDD_3.3V -> VDD
- C55 pad 1: /USB/VSYS_5V -> /Power/VSYS_5V
- C58 pad 1: /USB/VDD_3.3V -> VDD
- C6 pad 1: /DDR/VCC_DRAM_1.2V -> /DDR/NVCC_DRAM_1.2V
- C63 pad 1: /USB/VDD_3.3V -> VDD
- C64 pad 1: /USB/VDD_3.3V -> VDD
- C65 pad 1: /i.MX8MM Power/NVCC_SNVS_1.8V -> /Misc/NVCC_SNVS_1.8V
- C66 pad 1: /i.MX8MM Power/VDD_ARM_0.9V -> /Power/VDD_ARM_0.9V
- C67 pad 1: /i.MX8MM Power/VDD_SOC_0.8V -> /Power/VDD_SOC_0.8V
- C68 pad 1: /i.MX8MM Power/VDD_DRAM_xPU_0.9V -> /Power/VDD_DRAM_xPU_0.9V
- C69 pad 1: /i.MX8MM Power/NVCC_DRAM_1.2V -> /DDR/NVCC_DRAM_1.2V
- C70 pad 1: /i.MX8MM Power/VDDA_1.8V -> /Power/VDDA_1.8V
- C71 pad 1: /i.MX8MM Power/VDD_SNVS_0.8V -> /Misc/VDD_SNVS_0.8V
- C72 pad 1: /i.MX8MM Power/VDD_ARM_0.9V -> /Power/VDD_ARM_0.9V
- C73 pad 1: /i.MX8MM Power/VDD_SOC_0.8V -> /Power/VDD_SOC_0.8V
- C74 pad 1: /i.MX8MM Power/VDD_DRAM_xPU_0.9V -> /Power/VDD_DRAM_xPU_0.9V
- C75 pad 1: /i.MX8MM Power/NVCC_DRAM_1.2V -> /DDR/NVCC_DRAM_1.2V
- C76 pad 1: /i.MX8MM Power/VDD_ARM_0.9V -> /Power/VDD_ARM_0.9V
- C77 pad 1: /i.MX8MM Power/VDD_SOC_0.8V -> /Power/VDD_SOC_0.8V
- C78 pad 1: /i.MX8MM Power/VDD_DRAM_xPU_0.9V -> /Power/VDD_DRAM_xPU_0.9V
- C79 pad 1: /i.MX8MM Power/NVCC_DRAM_1.2V -> /DDR/NVCC_DRAM_1.2V
- C8 pad 1: /DDR/VCC_DRAM_1.2V -> /DDR/NVCC_DRAM_1.2V
- C80 pad 1: /i.MX8MM Power/VDDA_1.8V -> /Power/VDDA_1.8V
- C81 pad 1: /i.MX8MM Power/VDD_ARM_0.9V -> /Power/VDD_ARM_0.9V
- C82 pad 1: /i.MX8MM Power/VDD_SOC_0.8V -> /Power/VDD_SOC_0.8V
- C83 pad 1: /i.MX8MM Power/VDD_DRAM_xPU_0.9V -> /Power/VDD_DRAM_xPU_0.9V
- C84 pad 1: /i.MX8MM Power/NVCC_DRAM_1.2V -> /DDR/NVCC_DRAM_1.2V
- C85 pad 1: /i.MX8MM Power/VDD_ARM_0.9V -> /Power/VDD_ARM_0.9V
- C86 pad 1: /i.MX8MM Power/VDD_SOC_0.8V -> /Power/VDD_SOC_0.8V
- C87 pad 1: /i.MX8MM Power/VDD_DRAM_xPU_0.9V -> /Power/VDD_DRAM_xPU_0.9V
- C88 pad 1: /i.MX8MM Power/NVCC_DRAM_1.2V -> /DDR/NVCC_DRAM_1.2V
- C89 pad 1: /i.MX8MM Power/VDD_ARM_0.9V -> /Power/VDD_ARM_0.9V
- C9 pad 1: /DDR/VPP_2.5V -> /DDR/NVCC_DRAM_1.2V
- C90 pad 1: /i.MX8MM Power/VDD_SOC_0.8V -> /Power/VDD_SOC_0.8V
- C91 pad 1: /i.MX8MM Power/VDD_DRAM_xPU_0.9V -> /Power/VDD_DRAM_xPU_0.9V
- C92 pad 1: /i.MX8MM Power/NVCC_DRAM_1.2V -> /DDR/NVCC_DRAM_1.2V
- C93 pad 1: /i.MX8MM Power/VDD_DRAM_xPU_0.9V -> /Power/VDD_DRAM_xPU_0.9V
- C94 pad 1: /i.MX8MM Power/NVCC_DRAM_1.2V -> /DDR/NVCC_DRAM_1.2V
- C95 pad 1: /i.MX8MM Power/VDD_DRAM_xPU_0.9V -> /Power/VDD_DRAM_xPU_0.9V
- C96 pad 1: /i.MX8MM Power/NVCC_DRAM_1.2V -> /DDR/NVCC_DRAM_1.2V
- C97 pad 1: /i.MX8MM Power/NVCC_1.8V -> VCC
- C98 pad 1: /i.MX8MM Power/NVCC_1.8V -> VCC
- C99 pad 1: /i.MX8MM Power/NVCC_1.8V -> VCC
- D1 pad 1: GND -> Net-(D1-Pad1)
- J7 pad A6: unconnected-(J7-PadA6) -> /USB/USB4_DP
- J7 pad A7: unconnected-(J7-PadA7) -> /USB/USB4_DN
- J7 pad B6: unconnected-(J7-PadB6) -> /USB/USB4_DP
- J7 pad B7: unconnected-(J7-PadB7) -> /USB/USB4_DN
- J8 pad 1: Net-(J8-Pad1) -> GND
- J8 pad 10: unconnected-(J8-Pad10) -> Net-(J8-Pad10)
- J8 pad 15: Net-(J8-Pad1) -> GND
- J8 pad 21: Net-(J8-Pad1) -> GND
- J8 pad 27: Net-(J8-Pad1) -> GND
- J8 pad 3: Net-(J8-Pad1) -> GND
- J8 pad 33: Net-(J8-Pad1) -> GND
- J8 pad 39: Net-(J8-Pad1) -> GND
- J8 pad 45: Net-(J8-Pad1) -> GND
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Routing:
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- added copper zone on In1.Cu, net GND
- added copper zone on In6.Cu, net GND
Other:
- copper layers 6 -> 8

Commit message: fix ref desgigators, add table for dram config
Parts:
- added L401: 0.47uH, Inductor_SMD:L_1008_2520Metric, F.Cu at (86.0, 113.0)
- added L402: 0.47uH, Inductor_SMD:L_1008_2520Metric, F.Cu at (81.0, 109.2)
- added L403: 0.47uH, Inductor_SMD:L_1008_2520Metric, F.Cu at (76.1, 109.2)
- added L404: 1uH, Inductor_SMD:L_1008_2520Metric, F.Cu at (76.1, 113.0)
- added L405: 0.47uH, Inductor_SMD:L_1008_2520Metric, F.Cu at (86.0, 109.2)
- added L406: 0.47uH, Inductor_SMD:L_1008_2520Metric, F.Cu at (81.0, 113.0)
- added R206: 0R, Resistor_SMD:R_0402_1005Metric, F.Cu at (95.0, 110.4)
- added R207: 0R, Resistor_SMD:R_0402_1005Metric, F.Cu at (95.0, 108.4)
- added R208: 0R, Resistor_SMD:R_0402_1005Metric, F.Cu at (97.9, 110.4)
- added R209: 0R, Resistor_SMD:R_0402_1005Metric, F.Cu at (97.9, 108.4)
- J1001: renamed from J8; value Bus_M.2_Socket_M -> 1-2199230-6
- renumbered C116 to C1001, C117 to C1002, C118 to C1003, C119 to C1004, C120 to C1005, C121 to C1006, C124 to C1007, C125 to C1008, C122 to C1009, C123 to C1010, C126 to C1011, C127 to C1012, C137 to C1013, C138 to C1014, C1 to C201, C2 to C202, C3 to C203, C4 to C204, C5 to C205, C6 to C206, C7 to C207, C8 to C208, C9 to C209, C10 to C210, C11 to C211, C12 to C212, C65 to C301, C66 to C302, C67 to C303, C68 to C304, C69 to C305, C70 to C306, C71 to C307, C72 to C308, C73 to C309, C74 to C310, C75 to C311, C76 to C312, C77 to C313, C78 to C314, C79 to C315, C80 to C316, C81 to C317, C82 to C318, C83 to C319, C84 to C320, C85 to C321, C86 to C322, C87 to C323, C88 to C324, C89 to C325, C90 to C326, C91 to C327, C92 to C328, C93 to C329, C94 to C330, C95 to C331, C96 to C332, C139 to C333, C145 to C334, C140 to C335, C146 to C336, C141 to C337, C147 to C338, C148 to C339, C149 to C340, C97 to C341, C150 to C342, C151 to C343, C152 to C344, C98 to C345, C142 to C346, C153 to C347, C154 to C348, C155 to C349, C99 to C350, C156 to C351, C157 to C352, C100 to C353, C143 to C354, C158 to C355, C101 to C356, C144 to C357, C13 to C401, C14 to C402, C15 to C403, C16 to C404, C17 to C405, C18 to C406, C19 to C407, C20 to C408, C21 to C409, C22 to C410, C23 to C411, C24 to C412, C25 to C413, C26 to C414, C27 to C415, C28 to C416, C29 to C417, C30 to C418, C31 to C419, C32 to C420, C33 to C421, C34 to C422, C35 to C423, C36 to C424, C37 to C425, C38 to C426, C39 to C427, C40 to C428, C41 to C429, C42 to C430, C43 to C431, C44 to C432, C45 to C433, C46 to C434, C47 to C435, C48 to C436, C49 to C437, C55 to C501, C50 to C502, C56 to C503, C51 to C504, C57 to C505, C52 to C506, C58 to C507, C53 to C508, C59 to C509, C54 to C510, C60 to C511, C61 to C512, C128 to C513, C129 to C514, C62 to C515, C63 to C516, C64 to C517, C130 to C518, C102 to C601, C103 to C602, C104 to C603, C105 to C604, C106 to C605, C107 to C606, C108 to C607, C109 to C608, C110 to C609, C111 to C610, C112 to C611, C113 to C612, C114 to C613, C115 to C614, C131 to C701, C132 to C702, C133 to C703, C134 to C704, C135 to C705, C136 to C706, C159 to C801, C160 to C802, D3 to D1001, D1 to D501, D2 to D502, FB2 to FB501, FB1 to FB502, FB3 to FB503, FB4 to FB504, H5 to H1001, H1 to H101, H2 to H102, H3 to H103, H4 to H104, J2 to J501, J3 to J502, J1 to J503, J7 to J504, J4 to J601, J5 to J701, J6 to J801, R65 to R1001, R66 to R1002, R67 to R1003, R68 to R1004, R80 to R1005, R69 to R1006, R81 to R1007, R82 to R1008, R1 to R201, R3 to R202, R4 to R203, R5 to R204, R6 to R205, R2 to R210, R7 to R211, R8 to R212, R101 to R401, R9 to R402, R102 to R403, R103 to R404, R10 to R405, R11 to R406, R19 to R501, R12 to R502, R20 to R503, R21 to R504, R13 to R505, R14 to R506, R22 to R507, R15 to R508, R23 to R509, R16 to R510, R24 to R511, R17 to R512, R25 to R513, R18 to R514, R26 to R515, R27 to R516, R28 to R517, R29 to R518, R30 to R519, R31 to R520, R32 to R521, R33 to R522, R35 to R523, R38 to R524, R34 to R525, R40 to R526, R36 to R527, R70 to R528, R37 to R529, R71 to R530, R39 to R531, R41 to R532, R42 to R601, R43 to R602, R44 to R603, R45 to R604, R46 to R605, R47 to R606, R48 to R607, R49 to R608, R50 to R609, R51 to R610, R52 to R611, R53 to R612, R54 to R613, R55 to R614, R56 to R615, R57 to R616, R58 to R617, R59 to R618, R60 to R619, R61 to R620, R62 to R621, R63 to R622, R64 to R623, R72 to R701, R73 to R702, R74 to R703, R75 to R704, R76 to R705, R104 to R801, R105 to R802, R106 to R803, R107 to R804, R108 to R805, R83 to R806, R109 to R807, R84 to R808, R77 to R809, R110 to R810, R111 to R811, R112 to R812, R113 to R901, R78 to R902, R114 to R903, R79 to R904, R85 to R905, R86 to R906, R87 to R907, R88 to R908, R89 to R909, R90 to R910, R91 to R911, R92 to R912, R93 to R913, R94 to R914, R95 to R915, R96 to R916, R97 to R917, R98 to R918, R99 to R919, R100 to R920, SW2 to SW401, SW1 to SW801, TP1 to TP201, TP2 to TP202, TP3 to TP203, TP4 to TP401, TP5 to TP402, TP6 to TP403, TP7 to TP404, TP8 to TP405, TP9 to TP406, TP10 to TP407, TP11 to TP408, TP12 to TP409, TP13 to TP410, TP14 to TP411, TP15 to TP412, TP16 to TP413, TP17 to TP414, TP18 to TP415, TP19 to TP416, TP20 to TP417, TP22 to TP418, TP23 to TP419, TP21 to TP501, TP24 to TP801, TP25 to TP802, TP26 to TP803, TP27 to TP804, TP28 to TP805, U17 to U1001, U25 to U1002, U24 to U1003, U1 to U201, U3 to U202, U16 to U401, U2 to U501, U8 to U502, U5 to U503, U6 to U504, U19 to U505, U10 to U506, U7 to U507, U20 to U508, U9 to U509, U12 to U510, U26 to U511, U27 to U512, U22 to U513, U11 to U514, U4 to U515, U21 to U516, U23 to U517, U28 to U518, U29 to U519, U18 to U601, U14 to U602, U13 to U603, U30 to U701, U31 to U702, U15 to U703, U32 to U704, U33 to U705, Y3 to Y1001, Y1 to Y401, Y2 to Y601, Y4 to Y801
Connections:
- net /Misc/NVCC_SNVS_1.8V renamed /Misc/CLK_32K_OUT
- U201 pad L1: unconnected-(U1-PadL1) -> /DDR/DRAM_BG1
- U202 pad E9: GND -> Net-(R208-Pad1)
- U202 pad M9: GND -> Net-(R206-Pad2)
- U202 pad T7: unconnected-(U3-PadT7) -> Net-(R209-Pad1)
